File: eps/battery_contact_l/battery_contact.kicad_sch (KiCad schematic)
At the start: 12 parts, among them J1 Conn_01x01, J10 Conn_01x01, J2 Conn_01x01, J3 Conn_01x01, J4 Conn_01x01, J5 Conn_01x03, J6 Conn_01x03, J7 Conn_01x01, J8 Conn_01x01, J9 Conn_01x01

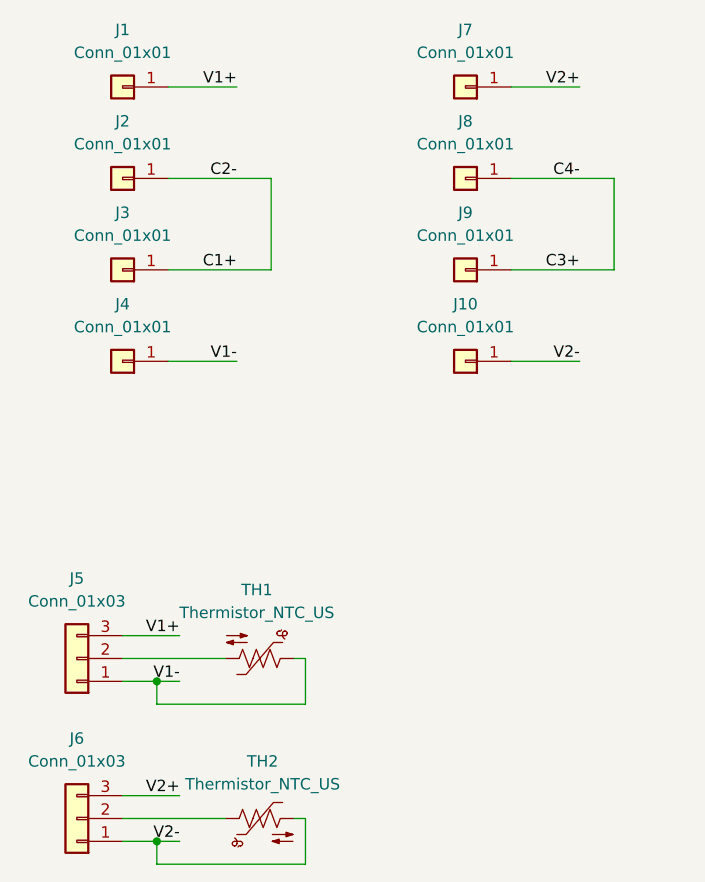
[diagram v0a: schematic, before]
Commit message: add battery contact PCBs
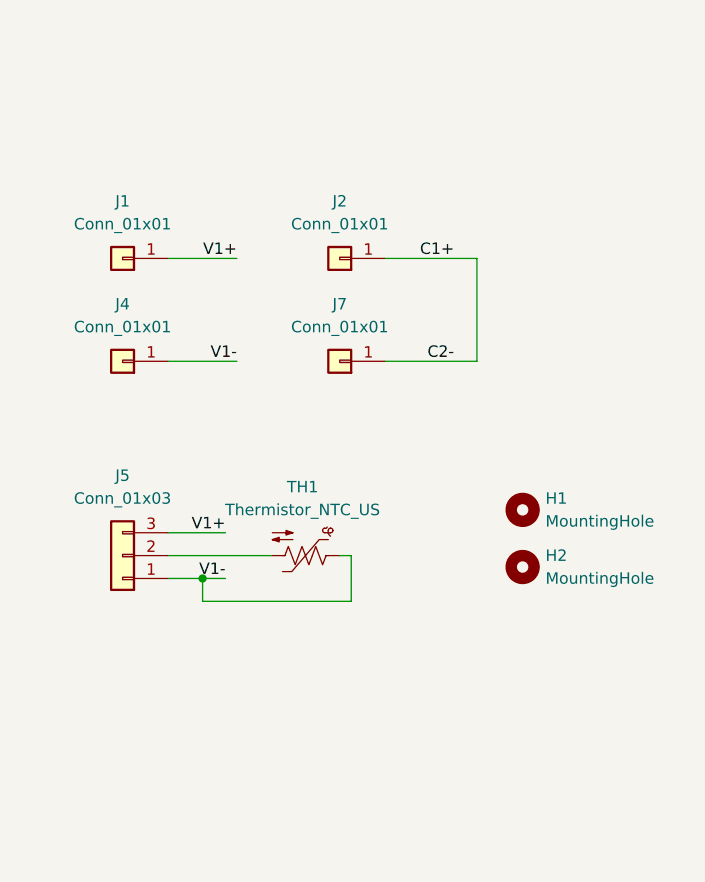
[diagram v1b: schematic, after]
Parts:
- removed J10, J3, J8, J9: Conn_01x01, footprints:BAT_FB07, symbol Connector_Generic:Conn_01x01
- removed J6: Conn_01x03, Connector_JST:JST_PH_B3B-PH-K_1x03_P2.00mm_Vertical, symbol Connector_Generic:Conn_01x03
- removed TH2: Thermistor_NTC_US, Resistor_SMD:R_0402_1005Metric, symbol Device:Thermistor_NTC_US
- added H1, H2: MountingHole, MountingHole:MountingHole_2.2mm_M2, symbol Mechanical:MountingHole
- J5: footprint Connector_JST:JST_PH_B3B-PH-K_1x03_P2.00mm_Vertical -> Connector_JST:JST_PH_B3B-PH-SM4-TB_1x03-1MP_P2.00mm_Vertical
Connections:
- net V2+ is gone; now on net C1+: J7.1 (Pin_1)
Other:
- moved on the sheet: J1, J5, TH1
